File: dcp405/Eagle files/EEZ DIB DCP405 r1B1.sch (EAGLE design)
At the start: 315 parts, among them IC1 LTC3864EMSE#PBF, IC10 MC33272ADR2G, IC11 MC33274ADR2G, IC12 LTC2050HVCS8#PBF, IC13 74AUP1G74DC.125, IC14 MCP23S17-E/SS, IC15 REF5025AIDR, IC16 DAC8552IDGKR, IC17 SN74LVC1G3157DCKR, IC18 ADS1120IPWR, IC19 LM339D, IC2 TL783CKCSE3, IC20 MAX9141ESA, IC3 LP2951SO8, IC4 SI8641BB-B-IS1, IC5 SN74LVC1G139DCUR, IC6 LTC3260EMSE#PBF, IC7 SI8641BB-B-IS1, IC8 M24C32-WMN6P, IC9 TMP1075AIDGK, J1 4907, J2 FCR7350R, J3 FCR7350B, K1 G6K-2F-5DC, Q1 IRFR5305, Q10 MMBT5551, Q11 MMBT5551, Q12 PSMN0R9-25YLC, Q13 PSMN0R9-25YLC, Q14 PSMN0R9-25YLC, Q15 2N7002, Q16 BSS84P, Q17 BTA26-600, Q18 FMMT493TA, Q19 2N7002, Q2 MMBT5401, Q20 2N7002, Q21 2N7002, Q22 MMBT5551, Q23 MMBT5401, Q24 MMBT5551, Q25 MMBT5551, Q26 2N7002, Q3 IRFP250MPBF, Q4 BC856C, Q5 BCP56-16.115, Q6 STF10P6F6, Q7 BCP56-16.115, Q8 MMBT5401, Q9 MMBT5401, X1 172648-0102, X2 M20-9701346, X3 1844249, X4 ZL263-20DG

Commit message: DCP405 BOM
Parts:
- IC11: value MC33274ADR2G -> MC33272ADR2G
- IC3: value LP2951SO8 -> LP2951
- KK1, KK2: value PCB-MB -> PCB-MB-01
- L1: value RN112-4-02 -> RN112-4-02-0M7
- Q1: value IRFR5305 -> SUD19P06-60
- R71: value 0R010 -> 0R010 (low TCR)
- X1: value 172648-0102 -> 39-30-1020
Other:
- note added: "I2C address: 0100 1XXX"
- note added: "I2C address: 1010 XXXX"
- note added: "Note 1.1: Possible alternative AUIRFR5305, IRFR5305, SPD30P06P or other with similar or lower input capacitance"
- note removed: "Note 1.1: Possible alternative AUIRFR5305, SUD19P06-60, SPD30P06P or other with similar or lower input capacitance"
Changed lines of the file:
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@@
 <part name="C58" library="rcl" deviceset="C-EU" device="C0603" value="100n"/>
 <part name="Q6" library="EEZ_Lib1" deviceset="P-MOSFET" device="MIRROR2" value="STF10P6F6"/>
-<part name="IC11" library="EEZ_Lib1" deviceset="TL072" device="SOIC8" value="MC33274ADR2G"/>
+<part name="IC11" library="EEZ_Lib1" deviceset="TL072" device="SOIC8" value="MC33272ADR2G"/>
 <part name="C40" library="rcl" deviceset="C-EU" device="C1206" value="1u/100V"/>
 <part name="P-1" library="supply2" deviceset="V-" device=""/>
@@
 <part name="SUPPLY54" library="supply2" deviceset="GND" device=""/>
 <part name="SUPPLY55" library="supply2" deviceset="GND" device=""/>
-<part name="KK1" library="EEZ_Lib1" deviceset="PCB-MB" device=""/>
-<part name="KK2" library="EEZ_Lib1" deviceset="PCB-MB" device=""/>
+<part name="KK1" library="EEZ_Lib1" deviceset="PCB-MB" device="" value="PCB-MB-01"/>
+<part name="KK2" library="EEZ_Lib1" deviceset="PCB-MB" device="" value="PCB-MB-01"/>
 <part name="C37" library="rcl" deviceset="C-EU" device="C0603" value="100n"/>
 <part name="C23" library="rcl" deviceset="C-EU" device="C0603" value="100n"/>
@@
 <part name="C38" library="rcl" deviceset="C-EU" device="C0603" value="100n"/>
 <part name="FRAME2" library="frames" deviceset="DINA4_L" device=""/>
-<part name="X1" library="EEZ_connectors" deviceset="MINIFIT_39301020" device="" value="172648-0102"/>
+<part name="X1" library="EEZ_connectors" deviceset="MINIFIT_39301020" device="" value="39-30-1020"/>
 <part name="RN2" library="EEZ_Lib1" deviceset="R_ARRAY4" device="" value="DR1206-33R-4/8"/>
 <part name="RN1" library="EEZ_Lib1" deviceset="R_ARRAY4" device="" value="DR1206-33R-4/8"/>
@@
 <part name="L3" library="EEZ_inductors_and_transformers" deviceset="COILCRAFT_HPI0630" device="" value="VLS6045AF-3R3N"/>
 <part name="SH3" library="EEZ_Lib1" deviceset="SHORT" device="NOHOLE" value="Sgnd to Pgnd short"/>
-<part name="Q1" library="EEZ_Lib1" deviceset="P-MOSFET" device="DPAK" value="IRFR5305"/>
+<part name="Q1" library="EEZ_Lib1" deviceset="P-MOSFET" device="DPAK" value="SUD19P06-60"/>
 <part name="IC1" library="EEZ_Lib1" deviceset="LTC3864" device="" value="LTC3864EMSE#PBF"/>
 <part name="C8" library="rcl" deviceset="C-EU" device="C0805" value="470n"/>
@@
 <part name="C21" library="rcl" deviceset="C-EU" device="C0603" value="100n"/>
 <part name="C22" library="EEZ_Lib1" deviceset="ECAP" device="1206" value="4u7"/>
-<part name="IC3" library="EEZ_Lib1" deviceset="LP2951" device="SO8"/>
+<part name="IC3" library="EEZ_Lib1" deviceset="LP2951" device="SO8" value="LP2951"/>
 <part name="R18" library="rcl" deviceset="R-EU_" device="R0805" value="16K"/>
 <part name="R19" library="rcl" deviceset="R-EU_" device="R0805" value="5K1"/>
@@
 <part name="R16" library="rcl" deviceset="R-EU_" device="R0805" value="1K8"/>
 <part name="C20" library="rcl" deviceset="CPOL-EU" device="C/6032-28R" value="1uF/50V Tant."/>
-<part name="L1" library="EEZ_Lib1" deviceset="RN112" device="" value="RN112-4-02"/>
+<part name="L1" library="EEZ_Lib1" deviceset="RN112" device="" value="RN112-4-02-0M7"/>
 <part name="ZD2" library="EEZ_Lib1" deviceset="ZENER-DIODE" device="SOD323" value="PDZ5.6B"/>
 <part name="R1" library="rcl" deviceset="R-EU_" device="R2512" value="4K7/2W"/>
@@
 <part name="R61" library="rcl" deviceset="R-EU_" device="R0805" value="47K"/>
 <part name="SUPPLY128" library="supply2" deviceset="GND" device="" value="GND"/>
-<part name="R71" library="EEZ_Lib1" deviceset="R-EU_4WIRE" device="H2728" value="0R010"/>
+<part name="R71" library="EEZ_Lib1" deviceset="R-EU_4WIRE" device="H2728" value="0R010 (low TCR)"/>
 <part name="PE1" library="supply1" deviceset="PE" device=""/>
 <part name="SUPPLY14" library="supply2" deviceset="GND" device=""/>
@@
 <text x="161.798" y="86.995" size="1.778" layer="96">100u</text>
 <text x="127" y="106.045" size="1.4224" layer="103">See Note 1.1</text>
-<text x="2.54" y="27.94" size="1.778" layer="103">Note 1.1: Possible alternative AUIRFR5305, SUD19P06-60, SPD30P06P or other with similar or lower input capacitance</text>
+<text x="2.54" y="27.94" size="1.778" layer="103">Note 1.1: Possible alternative AUIRFR5305, IRFR5305, SPD30P06P or other with similar or lower input capacitance</text>
 <text x="2.54" y="25.4" size="1.778" layer="103">Note 1.2: WE 7447709330, WE 7443551331, Coilcraft MSS1210-333, Coilcraft XAL1510-333, Vishay IHLP4040DZER470M11, etc.</text>
 <text x="2.54" y="22.86" size="1.778" layer="103">Note 1.3: Use 240K for 30 VAC main transformer</text>
@@
 <rectangle x1="111.76" y1="99.06" x2="116.84" y2="106.68" layer="97"/>
 <text x="56.515" y="171.45" size="1.27" layer="103">Step-down to ~12 V</text>
+<text x="26.035" y="24.765" size="1.27" layer="103">I2C address: 1010 XXXX</text>
+<text x="85.09" y="15.24" size="1.27" layer="103">I2C address: 0100 1XXX</text>
 </plain>
 <instances>
@@
 <wire x1="15.24" y1="101.6" x2="15.24" y2="104.14" width="0.1524" layer="91"/>
 <junction x="15.24" y="104.14"/>
-</segment>
-</net>
+<label x="15.24" y="140.335" size="1.27" layer="102"/>
+</segment>
+</net>

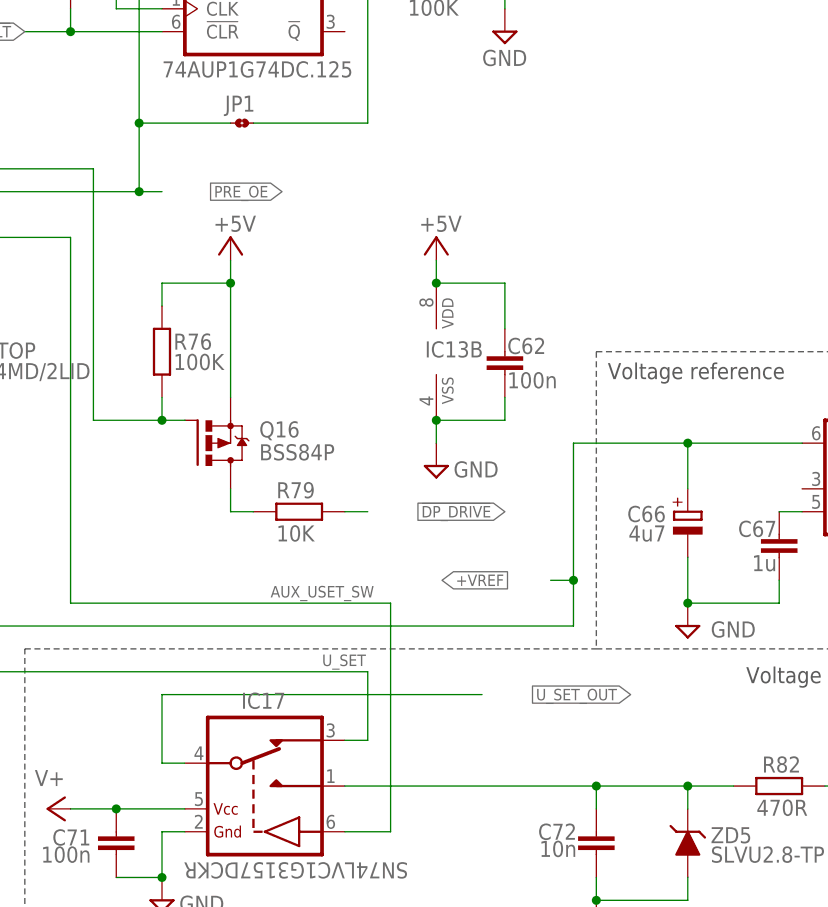
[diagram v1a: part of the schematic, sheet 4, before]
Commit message: DCP405 BOM update, JP2 added
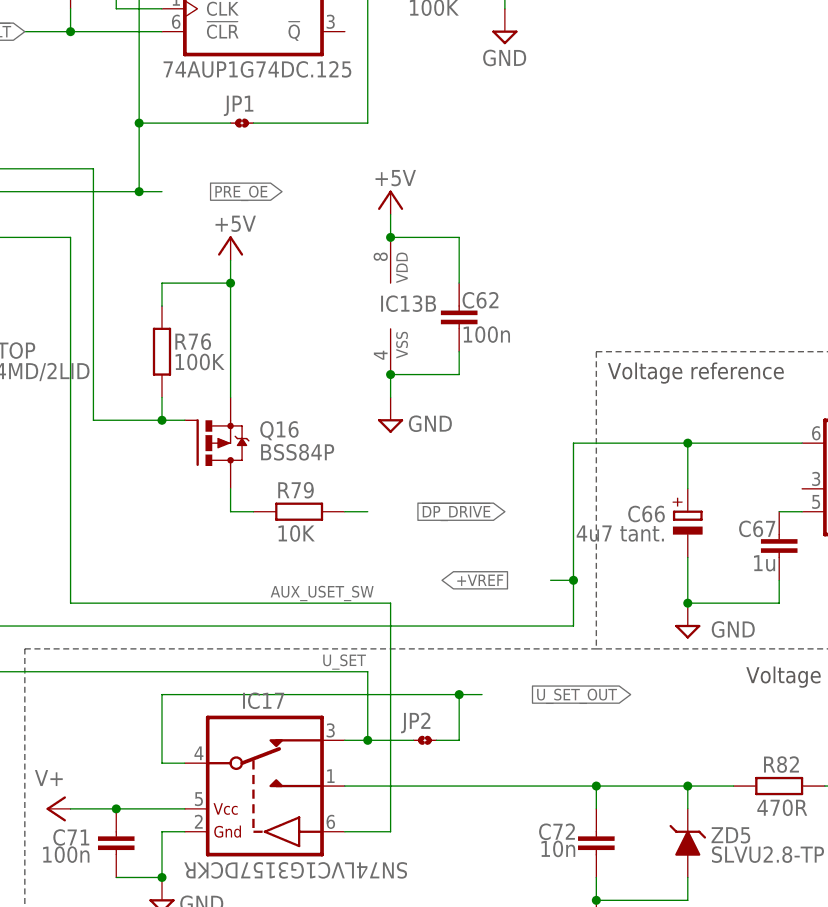
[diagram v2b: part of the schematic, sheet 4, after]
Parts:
- added D16: BAS316, EEZ_Lib1:DIODESOD323R
- added JP2: JP2-CUT, EEZ_Lib1:JP2-CUT
- C22, C66: value 4u7 -> 4u7 tant.
- C27, C34: value 10u -> 10u tant.
- D1: value STPS15H100 -> BAS316; device EEZ_Lib1:SCHOTTKY-DUAL_A_L -> EEZ_Lib1:DIODESOD323R
- D10: value SK55 -> BAS316; device EEZ_Lib1:SCHOTTKYSMB -> EEZ_Lib1:DIODESOD323R
- D11: value BAS316 -> SK55; device EEZ_Lib1:DIODESOD323R -> EEZ_Lib1:SCHOTTKYSMB
- D14: value SK10100D1-DIO -> BAS316; device EEZ_Lib1:SCHOTTKY-DUAL_A_L -> EEZ_Lib1:DIODESOD323R
- D15: value BAS316 -> SK10100D1-DIO; device EEZ_Lib1:DIODESOD323R -> EEZ_Lib1:SCHOTTKY-DUAL_A_L
- D2: value BAS316 -> STPS15H100; device EEZ_Lib1:DIODESOD323R -> EEZ_Lib1:SCHOTTKY-DUAL_A_L
- IC10: value MC33272ADR2G -> OPA2196ID
- R86: device rcl:R-EU_R0805 -> rcl:R-EU_R1206
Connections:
- removed net N$36: IC1.RUN, R2.1
- new net N$7: D1.C, IC1.RUN, R2.2
- net +5V: now also D16.C; no longer D15.C
- net GND: now also D14.C; no longer D13.C
- net I_SERVO: now also D10.C, D12.A; no longer D11.A, D9.C
- net LOOP_CTRL: now also D10.A, D8.A; no longer D7.A, D9.A
- net N$1: now also D3.C; no longer D2.C
- net N$114: now also D16.A; no longer D15.A
- net N$129: now also D7.C; no longer D6.C
- net N$143: now also D5.C; no longer D4.C
- net N$147: now also D6.A; no longer D5.A
- net N$20: now also D13.C, D14.A; no longer D12.C, D13.A
- net N$21: now also D13.A; no longer D12.A
- net N$79: now also D3.A; no longer D2.A
- net N$84: now also D9.C; no longer D8.C
- net N$89: now also D12.C; no longer D11.C
- net N$92: now also D4.C, D5.A; no longer D3.C, D4.A
- net N$93: now also D4.A; no longer D3.A
- net N$95: now also D7.A; no longer D6.A
- net POST_OUT-: now also D11.A, D15.A; no longer D10.A, D14.A
- net POST_OUTF+: now also D15.C; no longer D14.C
- net PREG_IN-: now also D2.A, R2.1; no longer D1.A
- net PREG_OUT-: now also D11.C; no longer D10.C
- net PRE_OE: now also D1.A; no longer R2.2
- net Q6C: now also D6.C; no longer D5.C
- net SW: now also D2.C; no longer D1.C
- net U_SERVO: now also D8.C, D9.A; no longer D7.C, D8.A
- net U_SET: now also JP2.1
- net U_SET_OUT: now also JP2.2
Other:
- note added: "Note 3.1: IC2, Q3 and Q6 mounted on heatsink"
- note removed: "Note 3.1: IC2, Q3 and Q4 mounted on heatsink"
- note removed: "Tant."
- moved on the sheet: C27, C34, C62, D13, D4, D5, D6, D7, D8, D9, IC13B, R2

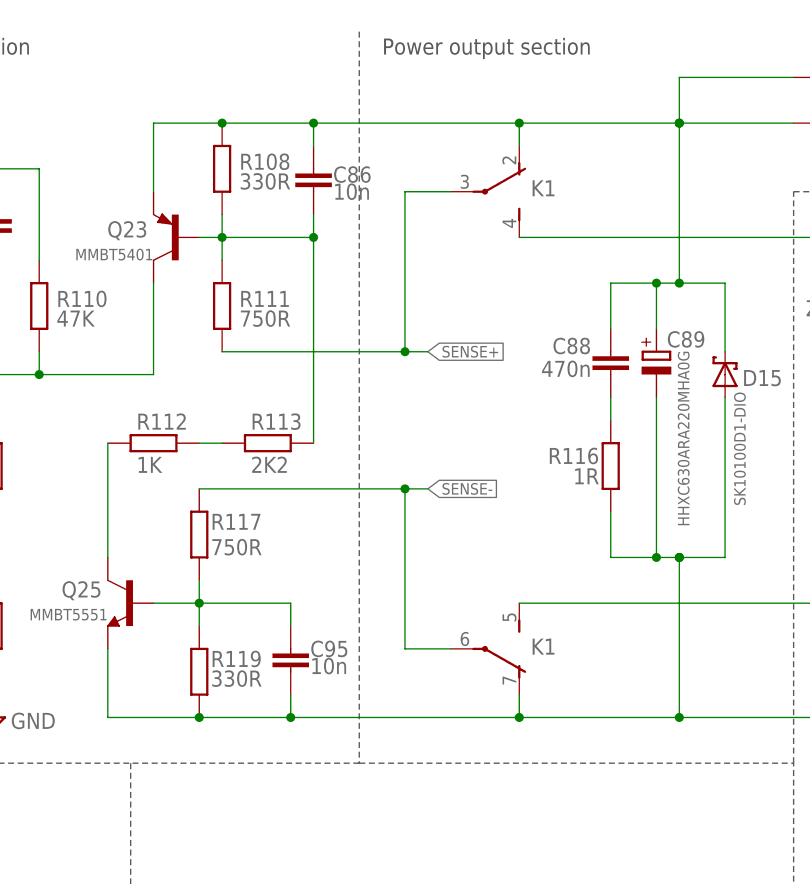
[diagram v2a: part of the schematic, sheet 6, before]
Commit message: DCP405 JP3, JP4 added
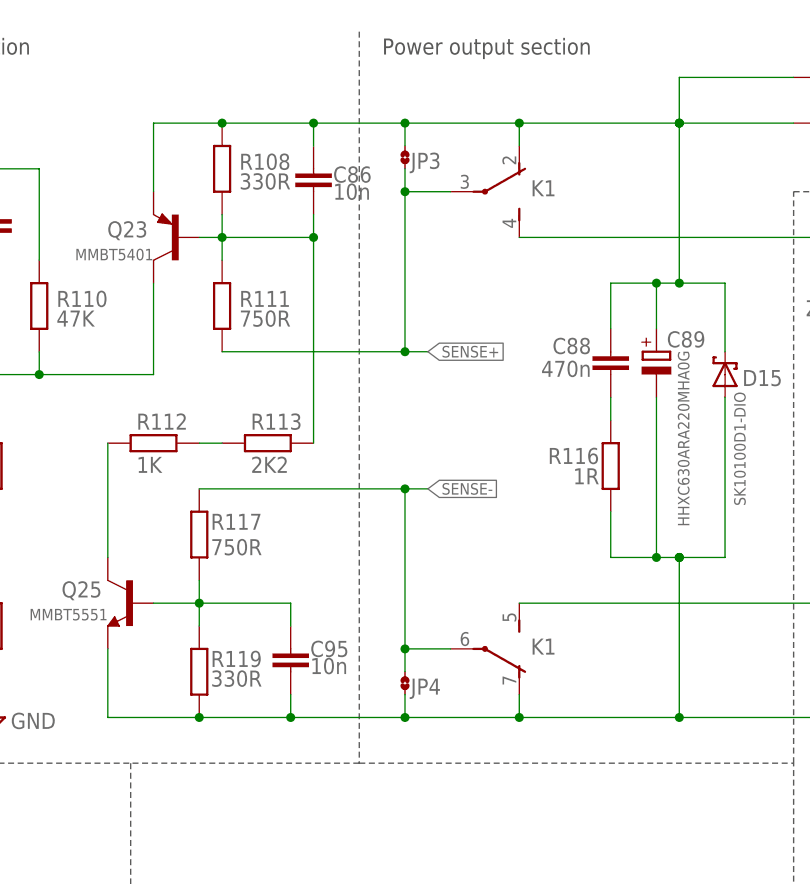
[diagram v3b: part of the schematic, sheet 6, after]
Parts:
- added JP3, JP4: JP2-CUT, EEZ_Lib1:JP2-CUT
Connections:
- net POST_OUT-: now also JP4.1
- net POST_OUTF+: now also JP3.2
- net SENSE+: now also JP3.1
- net SENSE-: now also JP4.2
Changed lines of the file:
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@@
 <setting verticaltext="up"/>
 </settings>
-<grid distance="0.1" unitdist="inch" unit="inch" style="lines" multiple="1" display="no" altdistance="0.01" altunitdist="inch" altunit="inch"/>
+<grid distance="0.1" unitdist="inch" unit="inch" style="lines" multiple="1" display="yes" altdistance="0.01" altunitdist="inch" altunit="inch"/>
 <layers>
 <layer number="1" name="Top" color="4" fill="1" visible="no" active="no"/>
@@
 <part name="D1" library="EEZ_Lib1" deviceset="DIODE" device="SOD323R" value="BAS316"/>
 <part name="JP2" library="EEZ_Lib1" deviceset="JP2-CUT" device=""/>
+<part name="JP3" library="EEZ_Lib1" deviceset="JP2-CUT" device=""/>
+<part name="JP4" library="EEZ_Lib1" deviceset="JP2-CUT" device=""/>
 </parts>
 <sheets>
@@
 <attribute name="VALUE" x="200.914" y="128.016" size="1.778" layer="96"/>
 </instance>
+<instance part="JP3" gate="G$1" x="93.98" y="162.56" smashed="yes" rot="R90">
+<attribute name="NAME" x="94.615" y="162.56" size="1.778" layer="95"/>
+</instance>
+<instance part="JP4" gate="G$1" x="93.98" y="104.14" smashed="yes" rot="R90">
+<attribute name="NAME" x="94.615" y="104.14" size="1.778" layer="95"/>
+</instance>
 </instances>
 <busses>
@@
 <wire x1="93.98" y1="160.02" x2="93.98" y2="142.24" width="0.1524" layer="91"/>
 <junction x="93.98" y="142.24"/>
+<pinref part="JP3" gate="G$1" pin="1"/>
+<wire x1="93.98" y1="162.56" x2="93.98" y2="160.02" width="0.1524" layer="91"/>
+<junction x="93.98" y="160.02"/>
 </segment>
 </net>
@@
 <wire x1="93.98" y1="109.22" x2="99.06" y2="109.22" width="0.1524" layer="91"/>
 <wire x1="71.12" y1="127" x2="93.98" y2="127" width="0.1524" layer="91"/>
+<pinref part="JP4" gate="G$1" pin="2"/>
+<wire x1="93.98" y1="109.22" x2="93.98" y2="106.68" width="0.1524" layer="91"/>
+<junction x="93.98" y="109.22"/>
 </segment>
 </net>
@@
 <wire x1="60.96" y1="101.6" x2="60.96" y2="109.22" width="0.1524" layer="91"/>
 <junction x="71.12" y="101.6"/>
-<wire x1="81.28" y1="101.6" x2="106.68" y2="101.6" width="0.1524" layer="91"/>
+<wire x1="81.28" y1="101.6" x2="93.98" y2="101.6" width="0.1524" layer="91"/>
 <junction x="81.28" y="101.6"/>
 <label x="175.26" y="101.6" size="1.27" layer="102" xref="yes"/>
 <pinref part="K1" gate="3" pin="O"/>
+<wire x1="93.98" y1="101.6" x2="106.68" y2="101.6" width="0.1524" layer="91"/>
 <wire x1="106.68" y1="101.6" x2="124.46" y2="101.6" width="0.1524" layer="91"/>
 <wire x1="124.46" y1="101.6" x2="160.02" y2="101.6" width="0.4064" layer="91"/>
@@
 <wire x1="121.92" y1="137.16" x2="121.92" y2="119.38" width="0.1524" layer="91"/>
 <junction x="121.92" y="119.38"/>
+<pinref part="JP4" gate="G$1" pin="1"/>
+<wire x1="93.98" y1="104.14" x2="93.98" y2="101.6" width="0.1524" layer="91"/>
+<junction x="93.98" y="101.6"/>
 </segment>
 </net>
@@
 <wire x1="73.66" y1="167.64" x2="83.82" y2="167.64" width="0.1524" layer="91"/>
 <wire x1="83.82" y1="167.64" x2="83.82" y2="165.1" width="0.1524" layer="91"/>
-<wire x1="83.82" y1="167.64" x2="106.68" y2="167.64" width="0.1524" layer="91"/>
+<wire x1="83.82" y1="167.64" x2="93.98" y2="167.64" width="0.1524" layer="91"/>
 <junction x="83.82" y="167.64"/>
 <pinref part="C88" gate="G$1" pin="1"/>
+<wire x1="93.98" y1="167.64" x2="106.68" y2="167.64" width="0.1524" layer="91"/>
 <wire x1="116.84" y1="149.86" x2="116.84" y2="144.78" width="0.1524" layer="91"/>
 <wire x1="124.46" y1="149.86" x2="121.92" y2="149.86" width="0.1524" layer="91"/>
@@
 <wire x1="121.92" y1="144.78" x2="121.92" y2="149.86" width="0.1524" layer="91"/>
 <junction x="121.92" y="149.86"/>
+<pinref part="JP3" gate="G$1" pin="2"/>
+<wire x1="93.98" y1="165.1" x2="93.98" y2="167.64" width="0.1524" layer="91"/>
+<junction x="93.98" y="167.64"/>
 </segment>
 </net>
